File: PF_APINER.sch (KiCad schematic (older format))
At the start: 0 parts

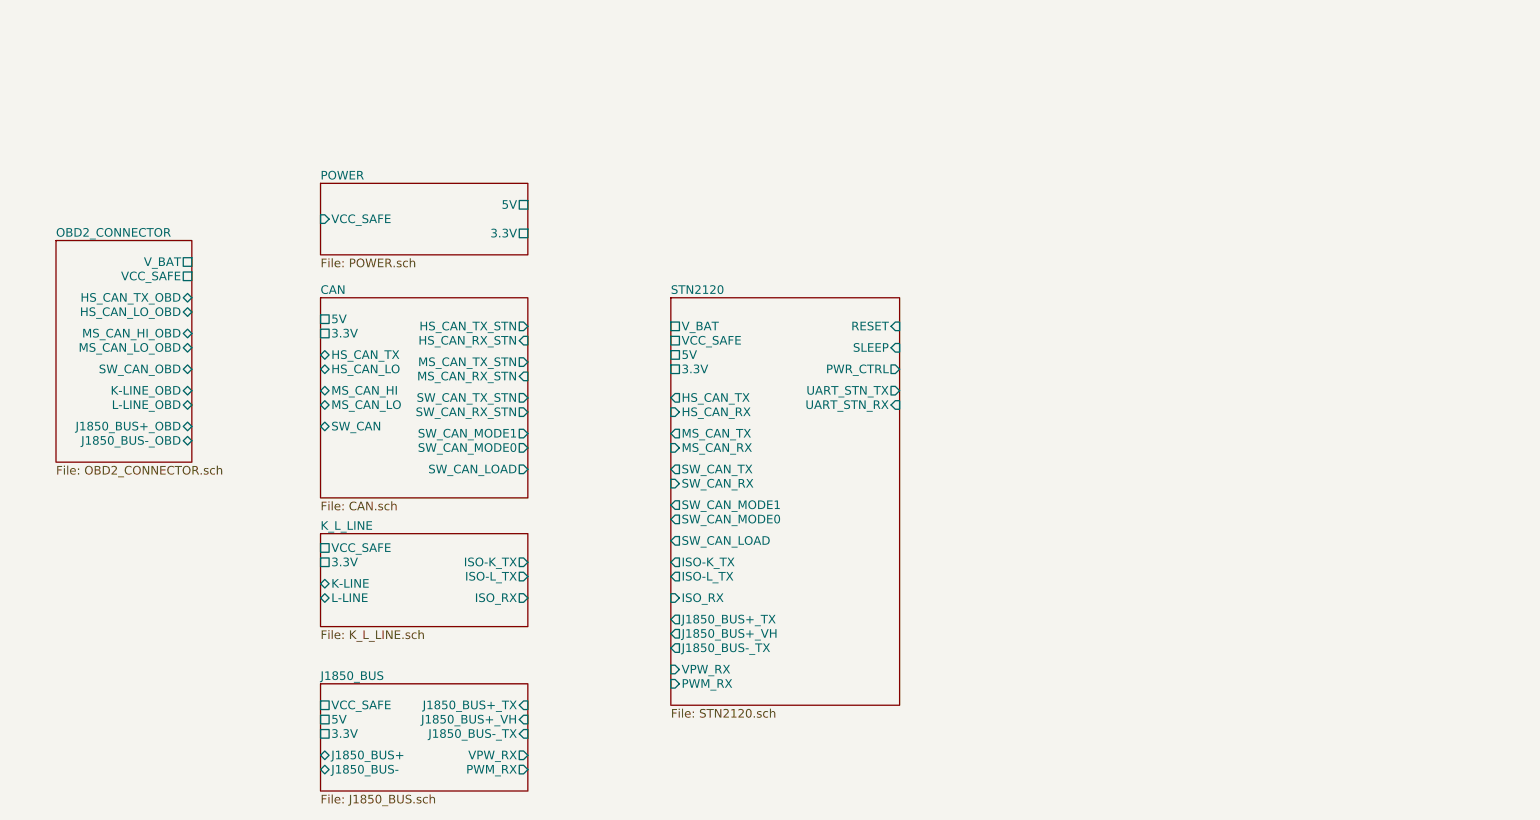
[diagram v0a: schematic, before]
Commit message: added uC
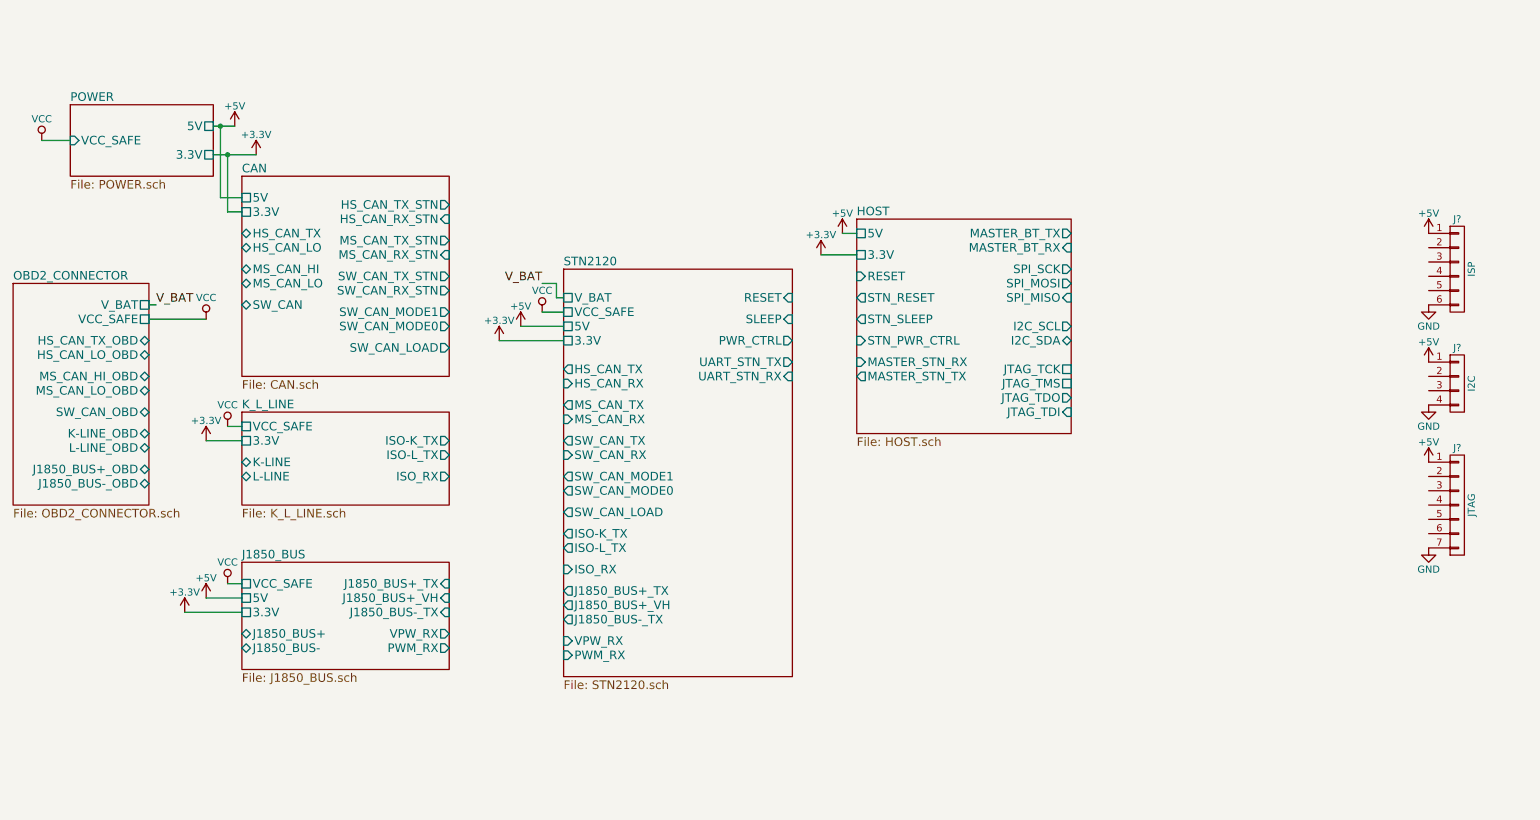
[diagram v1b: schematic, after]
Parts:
- added J?: JTAG, symbol CONN_01X07
- added J?: ISP, symbol CONN_01X06
- added J?: I2C, symbol CONN_01X04
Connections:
- new net +5V: J?.1 (P1), J?.1 (P1), J?.1 (P1)
- new net GND: J?.4 (P4), J?.6 (P6), J?.7 (P7)

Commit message: ready for first rev
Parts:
- added D? (x2): D, symbol D
- added J?: bluetooth, symbol CONN_01X04
- added R?: 1K, symbol R
- added R?: 2K, symbol R
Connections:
- net +5V: now also D?.1 (K), D?.1 (K), J?.1 (P1); no longer J?.1 (P1), J?.1 (P1)
- net GND: now also J?.2 (P2), R?.2
- net HOST/I2C_SCL: now also J?.2 (P2)
- net HOST/I2C_SDA: now also J?.3 (P3)
- net HOST/JTAG_TCK: now also J?.3 (P3)
- net HOST/JTAG_TDI: now also J?.6 (P6)
- net HOST/JTAG_TDO: now also J?.5 (P5)
- net HOST/JTAG_TMS: now also J?.4 (P4)
- net HOST/MASTER_BT_RX: now also J?.3 (P3)
- net HOST/MASTER_BT_TX: now also R?.1
- net HOST/SPI_MISO: now also J?.5 (P5)
- net HOST/SPI_MOSI: now also J?.4 (P4)
- net HOST/SPI_SCK: now also J?.3 (P3)
- net Host_RST: now reaches J?.2 (P2)
- net Host_RST: now also J?.2 (P2)
- new net: D?.2 (A), J?.1 (P1) (x2)
- new net: J?.4 (P4), R?.1, R?.2
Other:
- note added: "Solo el diodo de \nproteccion esta bien?\n"
- note added: "TX 3.3V lvl?"
- note added: "cambiar la coneccion de los pines\nen funcion del modulo"
- moved on the sheet: J?

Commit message: fixed some ports errors
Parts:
- gave numbers to parts that had none: 8
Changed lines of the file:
@@
 F1 "HOST.sch" 60
 F2 "5V" U L 6550 2050 60
-F3 "3.3V" U L 6550 2200 60
-F4 "MASTER_BT_RX" I R 8050 2150 60
-F5 "MASTER_BT_TX" O R 8050 2050 60
-F6 "MASTER_STN_RX" I L 6550 2950 60
-F7 "MASTER_STN_TX" O L 6550 3050 60
-F8 "RESET" I L 6550 2350 60
-F9 "SPI_MOSI" O R 8050 2400 60
-F10 "SPI_MISO" I R 8050 2500 60
-F11 "SPI_SCK" O R 8050 2300 60
-F12 "I2C_SCL" O R 8050 2700 60
-F13 "I2C_SDA" B R 8050 2800 60
-F14 "JTAG_TCK" U R 8050 3000 60
-F15 "JTAG_TMS" U R 8050 3100 60
-F16 "JTAG_TDO" O R 8050 3200 60
-F17 "JTAG_TDI" I R 8050 3300 60
-F18 "STN_RESET" O L 6550 2500 60
-F19 "STN_SLEEP" O L 6550 2650 60
-F20 "STN_PWR_CTRL" I L 6550 2800 60
+F3 "MASTER_BT_RX" I R 8050 2150 60
+F4 "MASTER_BT_TX" O R 8050 2050 60
+F5 "MASTER_STN_RX" I L 6550 2950 60
+F6 "MASTER_STN_TX" O L 6550 3050 60
+F7 "RESET" I L 6550 2350 60
+F8 "SPI_MOSI" O R 8050 2400 60
+F9 "SPI_MISO" I R 8050 2500 60
+F10 "SPI_SCK" O R 8050 2300 60
+F11 "I2C_SCL" O R 8050 2700 60
+F12 "I2C_SDA" B R 8050 2800 60
+F13 "JTAG_TCK" U R 8050 3000 60
+F14 "JTAG_TMS" U R 8050 3100 60
+F15 "JTAG_TDO" O R 8050 3200 60
+F16 "JTAG_TDI" I R 8050 3300 60
+F17 "STN_RESET" O L 6550 2500 60
+F18 "STN_SLEEP" O L 6550 2650 60
+F19 "STN_PWR_CTRL" I L 6550 2800 60
 $EndSheet
 $Comp
-L CONN_01X07 J?
+L CONN_01X07 J4
 U 1 1 5B0840F4
 P 10600 4700
-F 0 "J?" H 10600 5100 50  0000 C CNN
+F 0 "J4" H 10600 5100 50  0000 C CNN
 F 1 "JTAG" V 10700 4700 50  0000 C CNN
 F 2 "" H 10600 4700 50  0001 C CNN
@@
 $EndComp
 $Comp
-L CONN_01X06 J?
+L CONN_01X06 J2
 U 1 1 5B084CE9
 P 10550 2350
-F 0 "J?" H 10550 2700 50  0000 C CNN
+F 0 "J2" H 10550 2700 50  0000 C CNN
 F 1 "ISP" V 10650 2350 50  0000 C CNN
 F 2 "" H 10550 2350 50  0001 C CNN
@@
 $EndComp
 $Comp
-L CONN_01X04 J?
+L CONN_01X04 J3
 U 1 1 5B084F40
 P 10550 3300
-F 0 "J?" H 10550 3550 50  0000 C CNN
+F 0 "J3" H 10550 3550 50  0000 C CNN
 F 1 "I2C" V 10650 3300 50  0000 C CNN
 F 2 "" H 10550 3300 50  0001 C CNN
@@
 $EndComp
 $Comp
-L +5V #PWR?
+L +5V #PWR01
 U 1 1 5B090986
 P 2200 1300
-F 0 "#PWR?" H 2200 1150 50  0001 C CNN
+F 0 "#PWR01" H 2200 1150 50  0001 C CNN
 F 1 "+5V" H 2200 1440 50  0000 C CNN
 F 2 "" H 2200 1300 50  0001 C CNN
@@
 $EndComp
 $Comp
-L +3.3V #PWR?
+L +3.3V #PWR02
 U 1 1 5B090BB6
 P 2350 1500
-F 0 "#PWR?" H 2350 1350 50  0001 C CNN
+F 0 "#PWR02" H 2350 1350 50  0001 C CNN
 F 1 "+3.3V" H 2350 1640 50  0000 C CNN
 F 2 "" H 2350 1500 50  0001 C CNN
@@
 $EndComp
 $Comp
-L +5V #PWR?
+L +5V #PWR03
 U 1 1 5B097447
 P 10350 1750
-F 0 "#PWR?" H 10350 1600 50  0001 C CNN
+F 0 "#PWR03" H 10350 1600 50  0001 C CNN
 F 1 "+5V" H 10350 1890 50  0000 C CNN
 F 2 "" H 10350 1750 50  0001 C CNN
@@
 $EndComp
 $Comp
-L +5V #PWR?
+L +5V #PWR04
 U 1 1 5B09A0A1
 P 10350 3150
-F 0 "#PWR?" H 10350 3000 50  0001 C CNN
+F 0 "#PWR04" H 10350 3000 50  0001 C CNN
 F 1 "+5V" H 10350 3290 50  0000 C CNN
 F 2 "" H 10350 3150 50  0001 C CNN
@@
 $EndComp
 $Comp
-L GND #PWR?
+L GND #PWR05
 U 1 1 5B09EDE5
 P 10350 2600
-F 0 "#PWR?" H 10350 2350 50  0001 C CNN
+F 0 "#PWR05" H 10350 2350 50  0001 C CNN
 F 1 "GND" H 10350 2450 50  0000 C CNN
 F 2 "" H 10350 2600 50  0001 C CNN
@@
 $EndComp
 $Comp
-L GND #PWR?
+L GND #PWR06
 U 1 1 5B09FAAC
 P 10350 3450
-F 0 "#PWR?" H 10350 3200 50  0001 C CNN
+F 0 "#PWR06" H 10350 3200 50  0001 C CNN
 F 1 "GND" H 10350 3300 50  0000 C CNN
 F 2 "" H 10350 3450 50  0001 C CNN
@@
 $EndComp
 $Comp
-L GND #PWR?
+L GND #PWR07
 U 1 1 5B09FCD6
 P 10400 5000
-F 0 "#PWR?" H 10400 4750 50  0001 C CNN
+F 0 "#PWR07" H 10400 4750 50  0001 C CNN
 F 1 "GND" H 10400 4850 50  0000 C CNN
 F 2 "" H 10400 5000 50  0001 C CNN
@@
 $EndComp
 $Comp
-L VCC #PWR?
+L VCC #PWR08
 U 1 1 5B0B21E5
 P 1750 2650
-F 0 "#PWR?" H 1750 2500 50  0001 C CNN
+F 0 "#PWR08" H 1750 2500 50  0001 C CNN
 F 1 "VCC" H 1750 2800 50  0000 C CNN
 F 2 "" H 1750 2650 50  0001 C CNN
@@
 $EndComp
 $Comp
-L VCC #PWR?
+L VCC #PWR09
 U 1 1 5B0B2428
 P 850 1400
-F 0 "#PWR?" H 850 1250 50  0001 C CNN
+F 0 "#PWR09" H 850 1250 50  0001 C CNN
 F 1 "VCC" H 850 1550 50  0000 C CNN
 F 2 "" H 850 1400 50  0001 C CNN
@@
 $EndComp
 $Comp
-L VCC #PWR?
+L VCC #PWR010
 U 1 1 5B0B3B19
 P 2150 3400
-F 0 "#PWR?" H 2150 3250 50  0001 C CNN
+F 0 "#PWR010" H 2150 3250 50  0001 C CNN
 F 1 "VCC" H 2150 3550 50  0000 C CNN
 F 2 "" H 2150 3400 50  0001 C CNN
@@
 $EndComp
 $Comp
-L VCC #PWR?
+L VCC #PWR011
 U 1 1 5B0B3D55
 P 2150 4550
-F 0 "#PWR?" H 2150 4400 50  0001 C CNN
+F 0 "#PWR011" H 2150 4400 50  0001 C CNN
 F 1 "VCC" H 2150 4700 50  0000 C CNN
 F 2 "" H 2150 4550 50  0001 C CNN
@@
 $EndComp
 $Comp
-L VCC #PWR?
+L VCC #PWR012
 U 1 1 5B0B3F91
 P 4350 2600
-F 0 "#PWR?" H 4350 2450 50  0001 C CNN
+F 0 "#PWR012" H 4350 2450 50  0001 C CNN
 F 1 "VCC" H 4350 2750 50  0000 C CNN
 F 2 "" H 4350 2600 50  0001 C CNN
@@
 $EndComp
 $Comp
-L +3.3V #PWR?
+L +3.3V #PWR013
 U 1 1 5B0B7FEC
 P 1850 4750
-F 0 "#PWR?" H 1850 4600 50  0001 C CNN
+F 0 "#PWR013" H 1850 4600 50  0001 C CNN
 F 1 "+3.3V" H 1850 4890 50  0000 C CNN
 F 2 "" H 1850 4750 50  0001 C CNN
@@
 $EndComp
 $Comp
-L +5V #PWR?
+L +5V #PWR014
 U 1 1 5B0BA6A3
 P 2000 4650
-F 0 "#PWR?" H 2000 4500 50  0001 C CNN
+F 0 "#PWR014" H 2000 4500 50  0001 C CNN
 F 1 "+5V" H 2000 4790 50  0000 C CNN
 F 2 "" H 2000 4650 50  0001 C CNN
@@
 $EndComp
 $Comp
-L +5V #PWR?
+L +5V #PWR015
 U 1 1 5B0BCC00
 P 4200 2700
-F 0 "#PWR?" H 4200 2550 50  0001 C CNN
+F 0 "#PWR015" H 4200 2550 50  0001 C CNN
 F 1 "+5V" H 4200 2840 50  0000 C CNN
 F 2 "" H 4200 2700 50  0001 C CNN
@@
 $EndComp
 $Comp
-L +3.3V #PWR?
+L +3.3V #PWR016
 U 1 1 5B0BCE3C
 P 4050 2800
-F 0 "#PWR?" H 4050 2650 50  0001 C CNN
+F 0 "#PWR016" H 4050 2650 50  0001 C CNN
 F 1 "+3.3V" H 4050 2940 50  0000 C CNN
 F 2 "" H 4050 2800 50  0001 C CNN
@@
 $EndComp
 $Comp
-L +5V #PWR?
+L +5V #PWR017
 U 1 1 5B0C436B
 P 6450 2050
-F 0 "#PWR?" H 6450 1900 50  0001 C CNN
+F 0 "#PWR017" H 6450 1900 50  0001 C CNN
 F 1 "+5V" H 6450 2190 50  0000 C CNN
 F 2 "" H 6450 2050 50  0001 C CNN
@@
 $EndComp
 $Comp
-L +3.3V #PWR?
-U 1 1 5B0C45A7
-P 6300 2200
-F 0 "#PWR?" H 6300 2050 50  0001 C CNN
-F 1 "+3.3V" H 6300 2340 50  0000 C CNN
-F 2 "" H 6300 2200 50  0001 C CNN
-F 3 "" H 6300 2200 50  0001 C CNN
-	1    6300 2200
-	1    0    0    -1
-$EndComp
-$Comp
-L +3.3V #PWR?
+L +3.3V #PWR018
 U 1 1 5B0DC605
 P 2000 3500
-F 0 "#PWR?" H 2000 3350 50  0001 C CNN
+F 0 "#PWR018" H 2000 3350 50  0001 C CNN
 F 1 "+3.3V" H 2000 3640 50  0000 C CNN
 F 2 "" H 2000 3500 50  0001 C CNN
@@
 Host_RST
 $Comp
-L D D?
+L D D2
 U 1 1 5B0953C6
 P 10350 1900
-F 0 "D?" H 10350 2000 50  0000 C CNN
+F 0 "D2" H 10350 2000 50  0000 C CNN
 F 1 "D" H 10350 1800 50  0000 C CNN
 F 2 "" H 10350 1900 50  0001 C CNN
@@
 $EndComp
 $Comp
-L D D?
+L D D1
 U 1 1 5B0975AC
 P 10150 4300
-F 0 "D?" H 10150 4400 50  0000 C CNN
+F 0 "D1" H 10150 4400 50  0000 C CNN
 F 1 "D" H 10150 4200 50  0000 C CNN
 F 2 "" H 10150 4300 50  0001 C CNN
@@
 Solo el diodo de \nproteccion esta bien?\n
 $Comp
-L CONN_01X04 J?
+L CONN_01X04 J1
 U 1 1 5B20908F
 P 10500 950
-F 0 "J?" H 10500 1200 50  0000 C CNN
+F 0 "J1" H 10500 1200 50  0000 C CNN
 F 1 "bluetooth" V 10600 950 50  0000 C CNN
 F 2 "" H 10500 950 50  0001 C CNN
@@
 $EndComp
 $Comp
-L GND #PWR?
+L GND #PWR019
 U 1 1 5B20A149
 P 10150 900
-F 0 "#PWR?" H 10150 650 50  0001 C CNN
+F 0 "#PWR019" H 10150 650 50  0001 C CNN
 F 1 "GND" H 10150 750 50  0000 C CNN
 F 2 "" H 10150 900 50  0001 C CNN
@@
 $EndComp
 $Comp
-L +5V #PWR?
+L +5V #PWR020
 U 1 1 5B20A395
 P 10300 800
-F 0 "#PWR?" H 10300 650 50  0001 C CNN
+F 0 "#PWR020" H 10300 650 50  0001 C CNN
 F 1 "+5V" H 10300 940 50  0000 C CNN
 F 2 "" H 10300 800 50  0001 C CNN
@@
 TX 3.3V lvl?
 $Comp
-L +5V #PWR?
+L +5V #PWR021
 U 1 1 5B09B4B9
 P 9950 4100
-F 0 "#PWR?" H 9950 3950 50  0001 C CNN
+F 0 "#PWR021" H 9950 3950 50  0001 C CNN
 F 1 "+5V" H 9950 4240 50  0000 C CNN
 F 2 "" H 9950 4100 50  0001 C CNN
@@
 $EndComp
 $Comp
-L R R?
+L R R1
 U 1 1 5B25B0CA
 P 8850 1000
-F 0 "R?" V 8930 1000 50  0000 C CNN
+F 0 "R1" V 8930 1000 50  0000 C CNN
 F 1 "1K" V 8850 1000 50  0000 C CNN
 F 2 "" V 8780 1000 50  0001 C CNN
@@
 $EndComp
 $Comp
-L R R?
+L R R2
 U 1 1 5B25B38C
 P 8850 1400
-F 0 "R?" V 8930 1400 50  0000 C CNN
+F 0 "R2" V 8930 1400 50  0000 C CNN
 F 1 "2K" V 8850 1400 50  0000 C CNN
 F 2 "" V 8780 1400 50  0001 C CNN
@@
 $EndComp
 $Comp
-L GND #PWR?
+L GND #PWR022
 U 1 1 5B25C50E
 P 8850 1550
-F 0 "#PWR?" H 8850 1300 50  0001 C CNN
+F 0 "#PWR022" H 8850 1300 50  0001 C CNN
 F 1 "GND" H 8850 1400 50  0000 C CNN
 F 2 "" H 8850 1550 50  0001 C CNN
@@
 	6450 2050 6550 2050
 Wire Wire Line
-	6300 2200 6550 2200
-Wire Wire Line
 	2000 3500 2250 3500
